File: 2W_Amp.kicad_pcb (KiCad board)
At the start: 2 copper layers, 64.5 x 25 mm, 43 parts, among them J1 Power_In, P1 SMA, U1 OPA2674, U2 OPA2674

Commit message: some cleanup later...
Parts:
- P1: footprint Connector_Coaxial:SMA_Amphenol_901-143_Horizontal -> Sma:SMA_PINS
- P2: renamed from RF OUT; footprint Connector_Coaxial:SMA_Amphenol_901-143_Horizontal -> Sma:SMA_PINS
- moved P2 0.06 mm to (88.5, 64.0), turned to 180 degrees
- turned P1 to 0 degrees
- renumbered ADT4-1T to TR1, ADT1.5-1 to TR2
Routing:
- net Net-(U1A-V+): track 35.5 -> 27.2 mm, vias 9 -> 7
- net Net-(C5-Pad2): track 16.0 -> 21.5 mm
- net Net-(C9-Pad2): track 20.8 -> 23.0 mm
- net Net-(U2A-V+): track 21.7 -> 23.7 mm, vias 7 -> 5
- net GND: vias 154 -> 152

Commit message: yet some other small adjustments
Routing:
- net GND: track 11.5 -> 14.5 mm
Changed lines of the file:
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@@
 	)
 	(segment
-		(start 55.576 57.424)
-		(end 55.576 56.424)
+		(start 55.576 56.724)
+		(end 55.8 56.5)
 		(width 0.3)
 		(layer "F.Cu")
@@
 	)
 	(segment
-		(start 61 58)
-		(end 61.845 58)
+		(start 55.5 58)
+		(end 55.5 59)
 		(width 0.3)
 		(layer "F.Cu")
@@
 	)
 	(segment
-		(start 55.5 57.5)
-		(end 55.576 57.424)
+		(start 61 58)
+		(end 61.845 58)
 		(width 0.3)
 		(layer "F.Cu")
@@
 	)
 	(segment
+		(start 55.5 57)
+		(end 55.5 58)
+		(width 0.6)
+		(layer "F.Cu")
+		(net 2)
+	)
+	(segment
 		(start 55.5 58.5)
 		(end 54.9625 58.5)
+		(width 0.3)
+		(layer "F.Cu")
+		(net 2)
+	)
+	(segment
+		(start 55.0375 57.5)
+		(end 55.5 57.5)
 		(width 0.3)
 		(layer "F.Cu")
@@
 	)
 	(segment
-		(start 55.576 56.424)
+		(start 56 55)
 		(end 56 56)
 		(width 0.3)
@@
 	)
 	(segment
-		(start 55.5 57.5)
-		(end 55.0375 57.5)
+		(start 55.8 56.2)
+		(end 56 56)
 		(width 0.3)
 		(layer "F.Cu")
@@
 	)
 	(segment
-		(start 55.0375 57.5)
-		(end 54.5 58.0375)
+		(start 55.576 57.424)
+		(end 55.576 56.724)
+		(width 0.3)
+		(layer "F.Cu")
+		(net 2)
+	)
+	(segment
+		(start 55.5 57.5)
+		(end 55.576 57.424)
 		(width 0.3)
 		(layer "F.Cu")
@@
 		(width 0.3)
 		(layer "F.Cu")
+		(net 2)
+	)
+	(segment
+		(start 55.8 56.5)
+		(end 55.8 56.2)
+		(width 0.3)
+		(layer "F.Cu")
+		(net 2)
+	)
+	(segment
+		(start 54.5 58.0375)
+		(end 55.0375 57.5)
+		(width 0.3)
+		(layer "F.Cu")

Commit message: yet some other other small adjustments
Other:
- board text added: "RF In 10 dBm max"
- board text added: "RF Out"
- board text removed: "RF IN 10 dBm"
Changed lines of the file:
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@@
 		(descr "SMA with through-hole connections")
 		(property "Reference" "P2"
-			(at 0 4.75 0)
+			(at 1 -3.7 0)
 			(layer "F.SilkS")
 			(effects
@@
 		)
 	)
-	(gr_text "RF IN 10 dBm"
-		(at 32 59.5 0)
+	(gr_text "RF Out"
+		(at 87.2 60.4 0)
+		(layer "F.SilkS")
+		(effects
+			(font
+				(size 0.6 0.6)
+				(thickness 0.15)
+				(bold yes)
+			)
+			(justify left bottom)
+		)
+	)
+	(gr_text "RF In 10 dBm max"
+		(at 32 60 0)
 		(layer "F.SilkS")
 		(effects

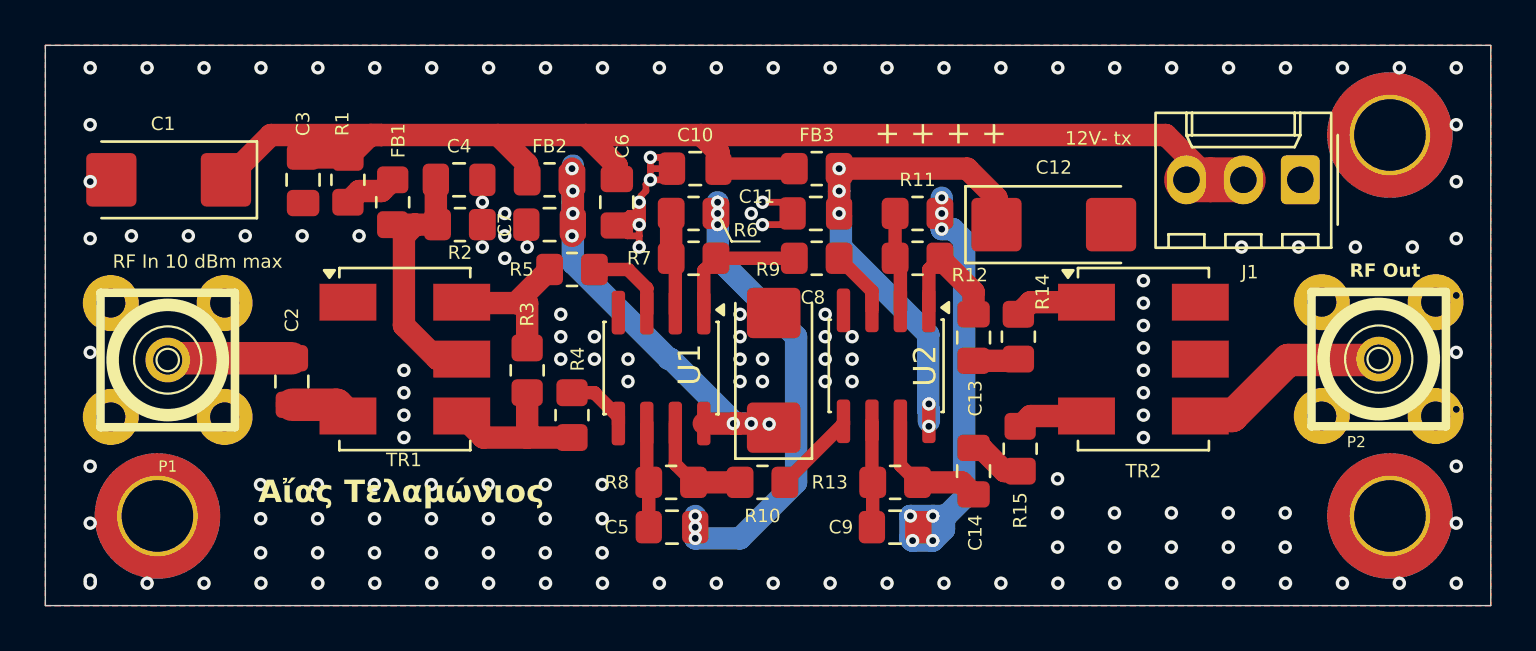
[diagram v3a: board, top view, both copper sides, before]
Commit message: decoupling on lower side, documentation added
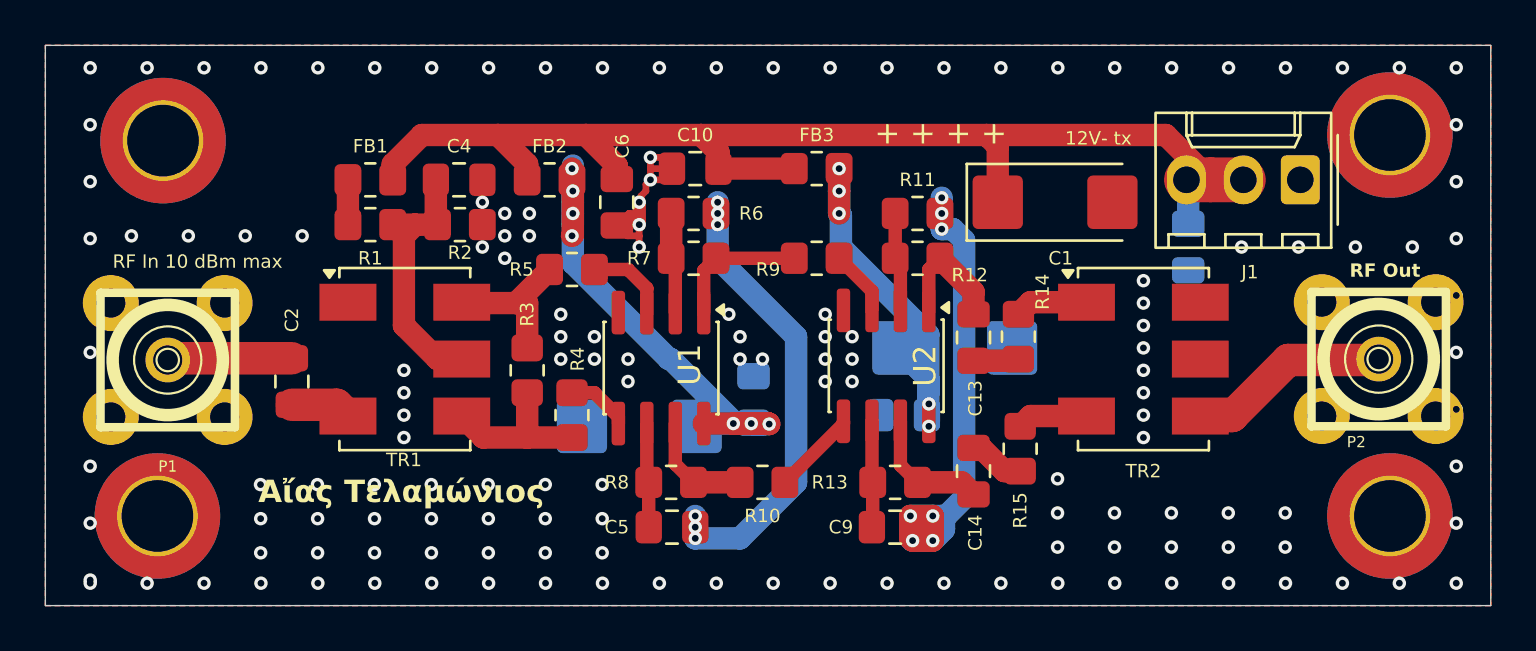
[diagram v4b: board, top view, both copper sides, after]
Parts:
- added H1: MountingHole_Pad, MountingHole:MountingHole_3.2mm_M3_DIN965_Pad_TopBottom, F.Cu at (34.2, 54.2)
- C11, C12, C3, C7, C8: moved to B.Cu
- moved C3 39.6 mm to (80.0, 59.0)
- moved C1 39.6 mm to (74.1, 57.0), turned to 0 degrees
- moved C7 12.0 mm to (60.6, 65.8), turned to 90 degrees
- moved C11 9.82 mm to (67.3, 66.5)
- moved C12 7.05 mm to (69.6, 63.5)
- moved C8 6.50 mm to (55.5, 67.0), turned to 180 degrees
- moved R1 1.41 mm to (43.5, 58.0), turned to 180 degrees
- moved FB1 1.00 mm to (43.5, 56.0), turned to 180 degrees
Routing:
- net Net-(U2A-V+): track 23.7 -> 17.5 mm
- net +12V: track 62.3 -> 56.6 mm
- net Net-(C9-Pad2): track 23.0 -> 27.2 mm
- net GND: track 14.5 -> 11.4 mm, vias 152 -> 147
- net Net-(U1A-V+): track 27.2 -> 28.3 mm
- net Net-(FB1-Pad2): track 2.41 -> 1.58 mm
